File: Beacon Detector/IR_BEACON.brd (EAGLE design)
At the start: 100 x 81.3 mm, 39 parts, among them U1 LP2950-3.0ACZ

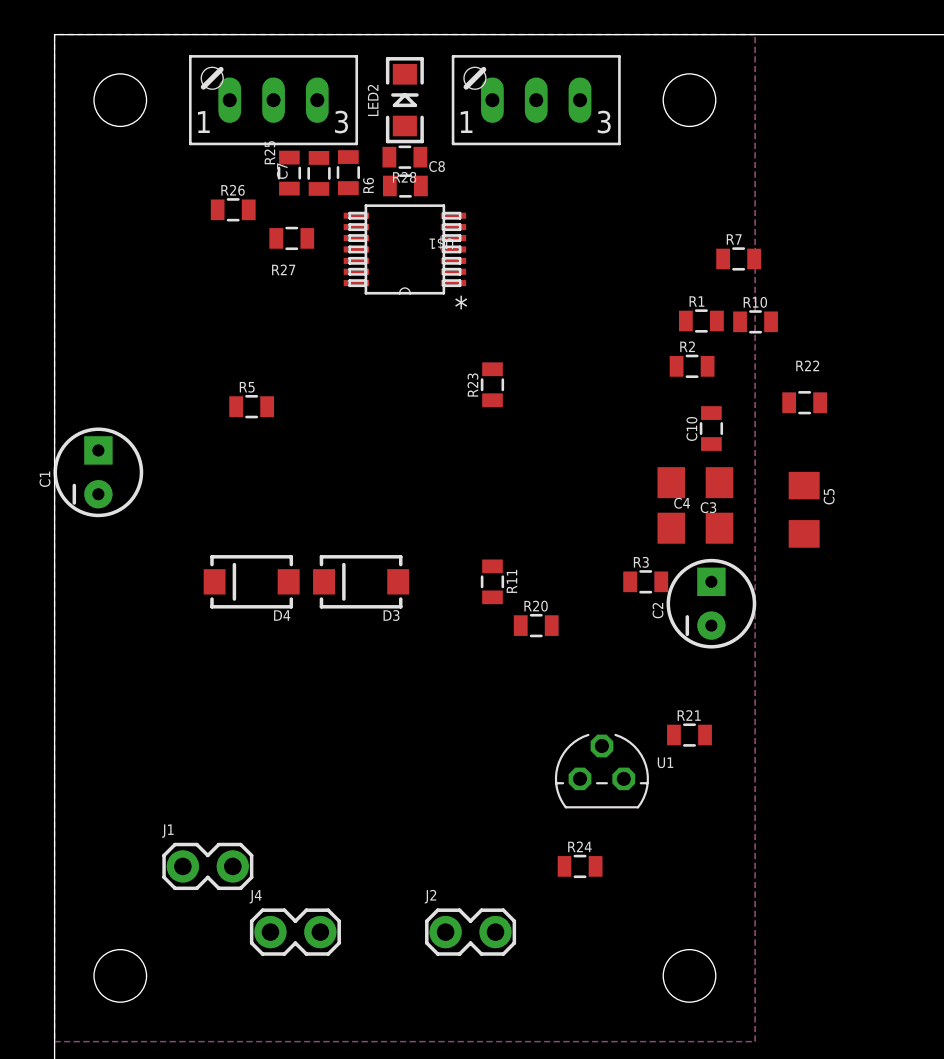
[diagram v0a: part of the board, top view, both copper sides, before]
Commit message: Added more to the beacon detector and finished the ring gears.
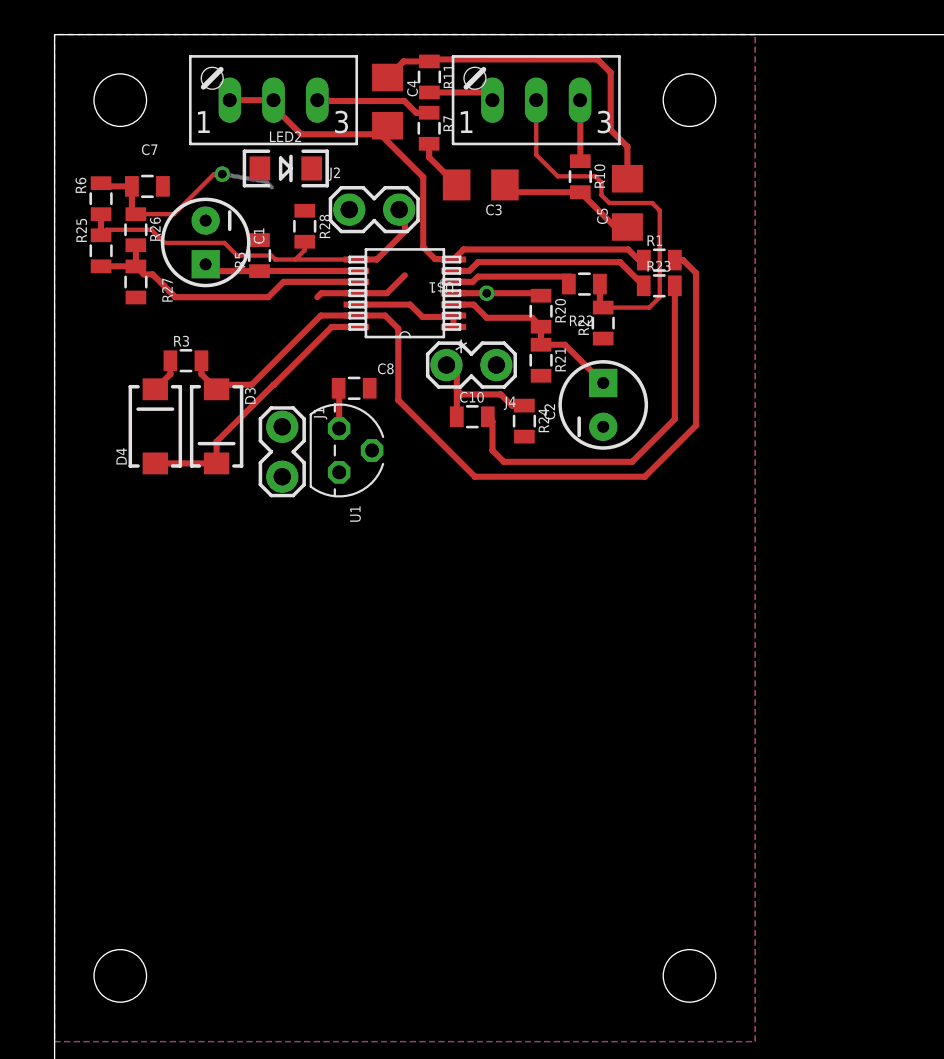
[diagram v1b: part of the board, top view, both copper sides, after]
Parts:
- moved J2 42.3 mm to (17.3, 69.8)
- moved J4 35.3 mm to (25.5, 60.8), turned to 180 degrees
- moved C4 30.5 mm to (19.3, 76.1), turned to 270 degrees
- moved R3 29.6 mm to (7.62, 61.1)
- moved R11 29.5 mm to (21.7, 77.5)
- moved R24 26.0 mm to (27.3, 57.6), turned to 270 degrees
- moved J1 25.9 mm to (13.2, 57.1), turned to 270 degrees
- moved U1 24.4 mm to (16.5, 55.9), turned to 270 degrees
- moved R21 23.4 mm to (28.2, 61.1), turned to 270 degrees
- moved C3 21.3 mm to (24.7, 71.3)
- moved C5 20.5 mm to (33.2, 70.2), turned to 90 degrees
- moved R7 19.5 mm to (21.7, 74.6), turned to 270 degrees
- moved R20 18.2 mm to (28.2, 64.0), turned to 270 degrees
- moved C1 14.7 mm to (8.76, 67.9), turned to 270 degrees
- moved R22 14.5 mm to (30.7, 65.5), turned to 180 degrees
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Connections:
- removed net V_OUT: J2.2, R25.2, R28.1, R6.2
- net N$1: now also D3.A, R1.2, R3.2, U$1.13; no longer R1.1
- net VOUTC: now also J2.2, R25.2, R28.1, R6.2
- net V_BIAS: now also U$1.12
- net V_FILT: now also R1.1; no longer D3.A, R1.2, R3.2
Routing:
- net N$1: track 0.00 -> 49.5 mm
- net V_FILT: track 0.00 -> 31.7 mm
- net V_BIAS: track 0.00 -> 28.7 mm
- net VOUTC: track 0.00 -> 23.0 mm
- net N$20: track 0.00 -> 21.7 mm
- net N$8: track 0.00 -> 20.3 mm
- net VCC: track 0.00 -> 20.1 mm, vias 0 -> 2
- net VINC+: track 0.00 -> 17.1 mm
- net N$15: track 0.00 -> 15.7 mm
- net N$4: track 0.00 -> 14.9 mm
- net N$16: track 0.00 -> 11.2 mm
- net V_ENV1: track 0.00 -> 8.91 mm
- net N$7: track 0.00 -> 8.11 mm
- net V_IR: track 0.00 -> 7.55 mm
- net N$19: track 0.00 -> 7.35 mm
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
